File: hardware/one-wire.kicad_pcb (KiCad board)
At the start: 2 copper layers, 30 x 30 mm, 28 parts, among them P1 CON-SENSOR2, P2 DEBUG, P3 BOOT, P4 CONN_02X03, P5 CONN_01X03, U1 XMC1100-16, U2 NC7WZ07, U3 DRILL, U4 DRILL, U5 DRILL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

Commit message: add z diode hint
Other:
- board text added: "5.6V SOD80?"
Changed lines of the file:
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@@
-(kicad_pcb (version 4) (host pcbnew 4.0.2+dfsg1-stable)
+(kicad_pcb (version 4) (host pcbnew 4.0.7-e2-6376~61~ubuntu18.04.1)
   (general
     (links 56)
     (no_connects 0)
-    (area 132.109499 109.509499 162.490501 139.890501)
+    (area 11.95714 108.844999 163.155001 195.615)
     (thickness 1.6)
-    (drawings 20)
+    (drawings 21)
     (tracks 205)
     (zones 0)
@@
     )
   )
+  (gr_text "5.6V SOD80?" (at 149.9 128.1) (layer Dwgs.User)
+    (effects (font (size 2.032 1.524) (thickness 0.3048)))
+  )
   (gr_text VCC (at 139.9 115.3 90) (layer F.SilkS)

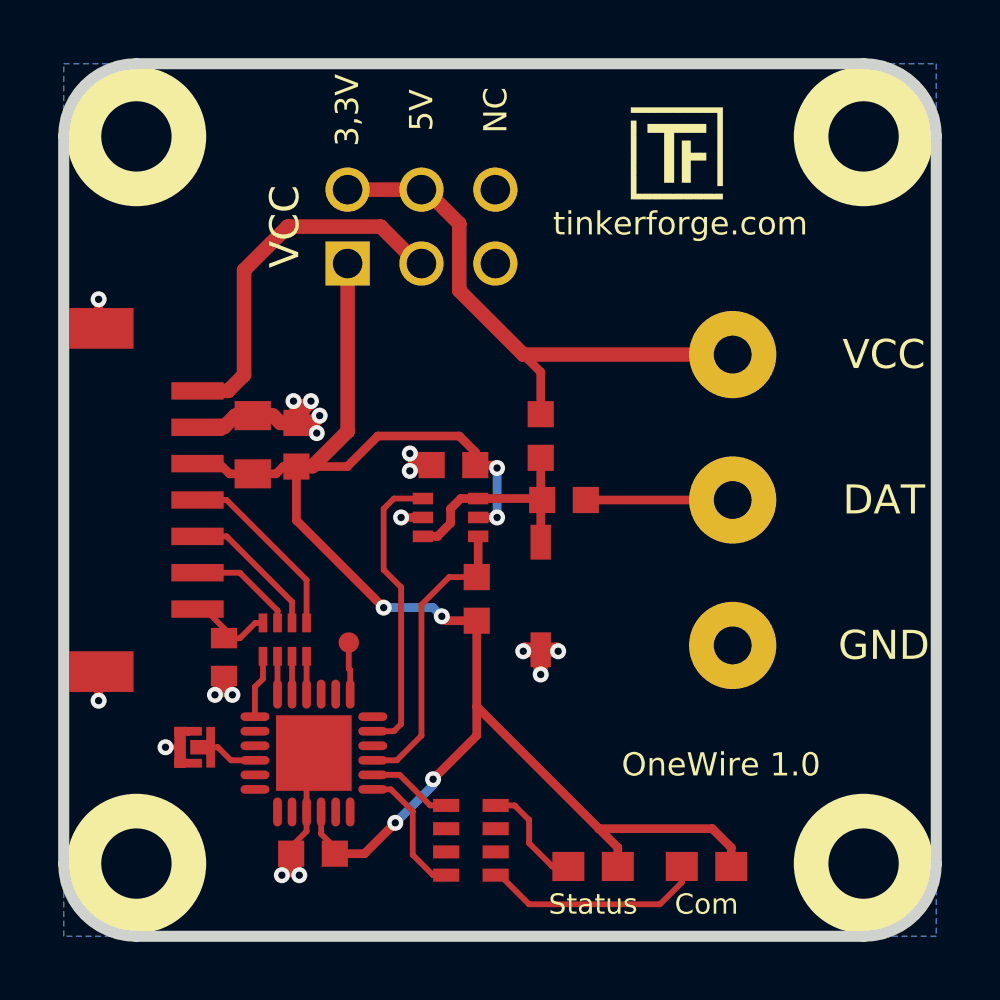
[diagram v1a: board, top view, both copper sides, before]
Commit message: set origin, specify zener
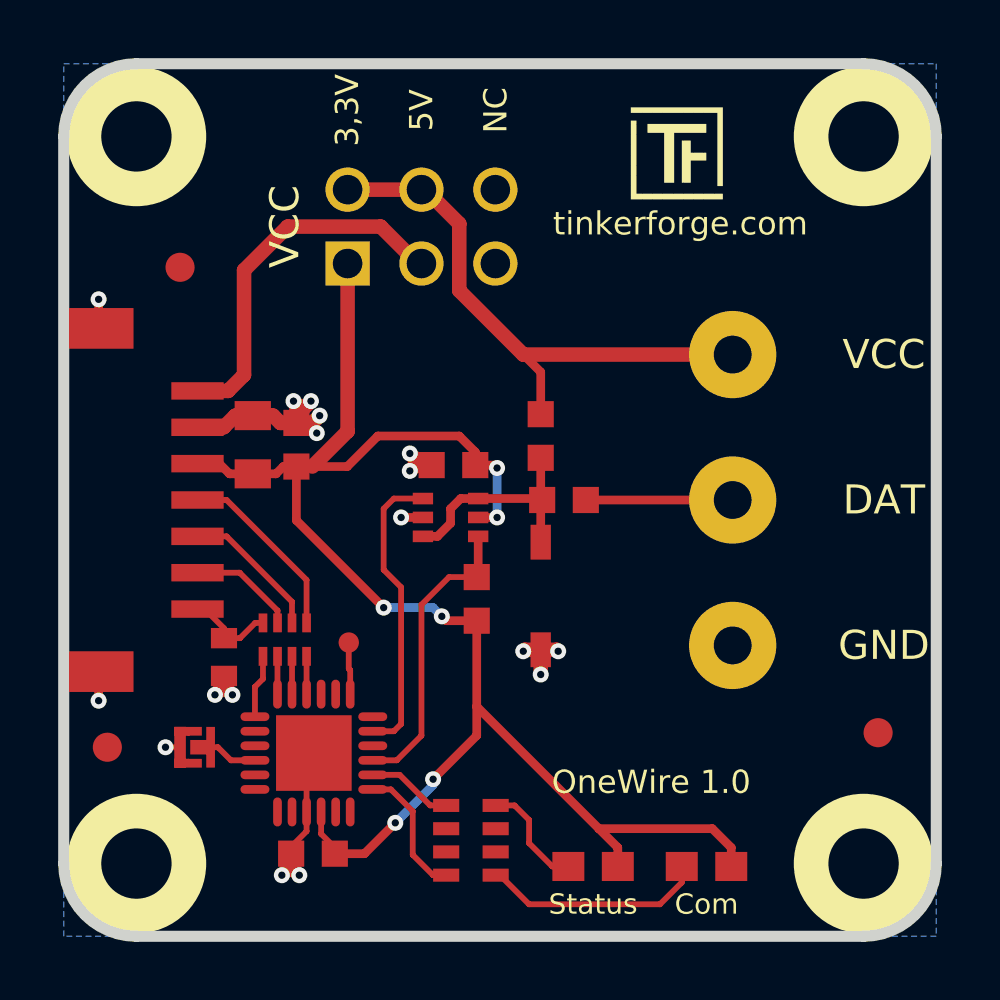
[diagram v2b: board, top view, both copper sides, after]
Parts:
- added Fiducial_Mark: VAL**, kicad-libraries:Fiducial_Mark, F.Cu at (136.3, 116.7)
- added Fiducial_Mark: VAL**, kicad-libraries:Fiducial_Mark, F.Cu at (160.3, 132.7)
- added Fiducial_Mark: VAL**, kicad-libraries:Fiducial_Mark, F.Cu at (133.8, 133.2)
- D2: value ZENER -> 5V
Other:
- board text removed: "5.6V SOD80?"
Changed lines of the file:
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@@
     (area 11.95714 108.844999 163.155001 195.615)
     (thickness 1.6)
-    (drawings 21)
+    (drawings 20)
     (tracks 205)
     (zones 0)
-    (modules 28)
+    (modules 31)
     (nets 23)
   )
@@
   (layers
     (0 F.Cu signal)
-    (31 B.Cu signal)
+    (31 B.Cu signal hide)
     (32 B.Adhes user)
     (33 F.Adhes user)
@@
     (pad_drill 0.6)
     (pad_to_mask_clearance 0)
-    (aux_axis_origin 0 0)
-    (visible_elements FFFFFF7F)
+    (aux_axis_origin 132.3 109.7)
+    (grid_origin 132.3 109.7)
+    (visible_elements FFFF7F7F)
     (pcbplotparams
       (layerselection 0x00010_00000000)
@@
       (effects (font (size 0.2 0.2) (thickness 0.05)))
     )
-    (fp_text value ZENER (at -0.5 -0.54 90) (layer F.Fab)
+    (fp_text value 5V (at -0.5 -0.54 90) (layer F.Fab)
       (effects (font (size 0.2 0.2) (thickness 0.05)))
     )
@@
     )
   )
-  (gr_text "5.6V SOD80?" (at 149.9 128.1) (layer Dwgs.User)
-    (effects (font (size 2.032 1.524) (thickness 0.3048)))
+  (module kicad-libraries:Fiducial_Mark (layer F.Cu)
+    (at 136.3 116.7)
+    (attr smd)
+    (fp_text reference Fiducial_Mark (at 0 0) (layer F.SilkS) hide
+      (effects (font (size 0.127 0.127) (thickness 0.03302)))
+    )
+    (fp_text value VAL** (at 0 -0.29972) (layer F.SilkS) hide
+      (effects (font (size 0.127 0.127) (thickness 0.03302)))
+    )
+    (fp_circle (center 0 0) (end 1.15062 0) (layer Dwgs.User) (width 0.01016))
+    (pad 1 smd circle (at 0 0) (size 1.00076 1.00076) (layers F.Cu F.Paste F.Mask)
+      (clearance 0.65024))
+  )
+  (module kicad-libraries:Fiducial_Mark (layer F.Cu)
+    (at 160.3 132.7)
+    (attr smd)
+    (fp_text reference Fiducial_Mark (at 0 0) (layer F.SilkS) hide
+      (effects (font (size 0.127 0.127) (thickness 0.03302)))
+    )
+    (fp_text value VAL** (at 0 -0.29972) (layer F.SilkS) hide
+      (effects (font (size 0.127 0.127) (thickness 0.03302)))
+    )
+    (fp_circle (center 0 0) (end 1.15062 0) (layer Dwgs.User) (width 0.01016))
+    (pad 1 smd circle (at 0 0) (size 1.00076 1.00076) (layers F.Cu F.Paste F.Mask)
+      (clearance 0.65024))
+  )
+  (module kicad-libraries:Fiducial_Mark (layer F.Cu)
+    (at 133.8 133.2)
+    (attr smd)
+    (fp_text reference Fiducial_Mark (at 0 0) (layer F.SilkS) hide
+      (effects (font (size 0.127 0.127) (thickness 0.03302)))
+    )
+    (fp_text value VAL** (at 0 -0.29972) (layer F.SilkS) hide
+      (effects (font (size 0.127 0.127) (thickness 0.03302)))
+    )
+    (fp_circle (center 0 0) (end 1.15062 0) (layer Dwgs.User) (width 0.01016))
+    (pad 1 smd circle (at 0 0) (size 1.00076 1.00076) (layers F.Cu F.Paste F.Mask)
+      (clearance 0.65024))
   )
   (gr_text VCC (at 139.9 115.3 90) (layer F.SilkS)
@@
     (effects (font (size 0.8 0.8) (thickness 0.15)))
   )
-  (gr_text "OneWire 1.0" (at 154.9 133.8) (layer F.SilkS)
+  (gr_text "OneWire 1.0" (at 152.5 134.4) (layer F.SilkS)
     (effects (font (size 0.8 0.8) (thickness 0.15)))
   )

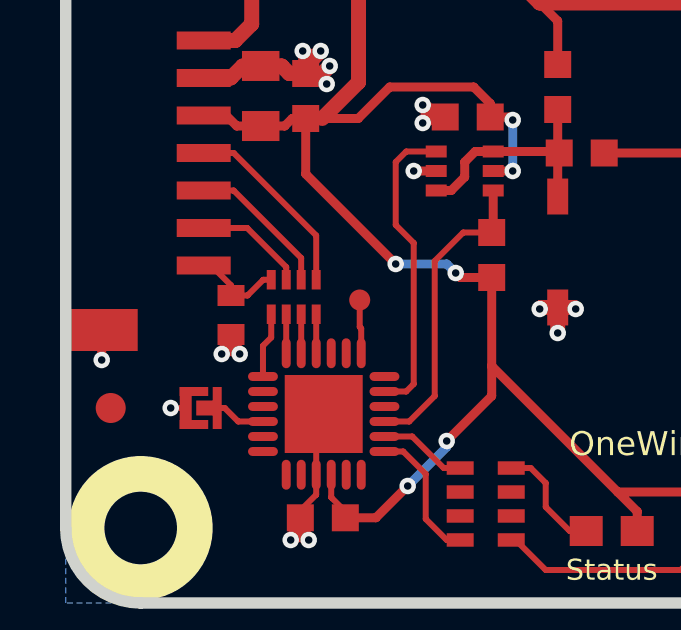
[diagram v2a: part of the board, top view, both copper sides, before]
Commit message: Change capacitor footprint(s) to C0402F
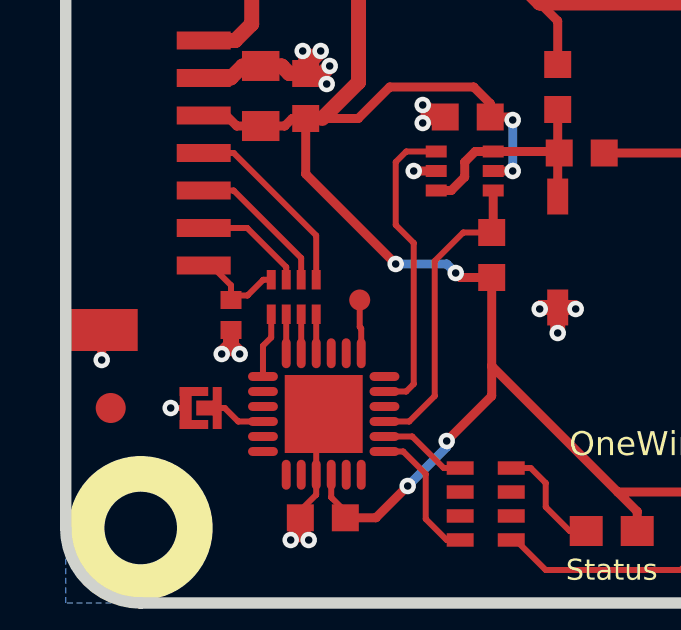
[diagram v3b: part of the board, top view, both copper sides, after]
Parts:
- C2: footprint kicad-libraries:C0402E -> kicad-libraries:C0402F
- R1: footprint R0603F -> kicad-libraries:R0603F
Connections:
- P4 pad 5: (no net) -> Net-(P4-Pad5)
- P4 pad 6: (no net) -> Net-(P4-Pad6)
- RP2 pad 2: (no net) -> Net-(RP2-Pad2)
- RP2 pad 3: (no net) -> Net-(RP2-Pad3)
- RP2 pad 6: (no net) -> Net-(RP2-Pad6)
- RP2 pad 7: (no net) -> Net-(RP2-Pad7)
- U1 pad 11: (no net) -> Net-(U1-Pad11)
- U1 pad 12: (no net) -> Net-(U1-Pad12)
- U1 pad 16: (no net) -> Net-(U1-Pad16)
- U1 pad 18: (no net) -> Net-(U1-Pad18)
- U1 pad 2: (no net) -> Net-(U1-Pad2)
- U1 pad 20: (no net) -> Net-(U1-Pad20)
- U1 pad 21: (no net) -> Net-(U1-Pad21)
- U1 pad 3: (no net) -> Net-(U1-Pad3)
- U1 pad 5: (no net) -> Net-(U1-Pad5)
- U1 pad 6: (no net) -> Net-(U1-Pad6)
- U1 pad 7: (no net) -> Net-(U1-Pad7)
- U1 pad 8: (no net) -> Net-(U1-Pad8)

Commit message: respecify processor XMC1100 -> 1300
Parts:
- U1: value XMC1100-16 -> XMC13XX24
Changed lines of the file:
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@@
-(kicad_pcb (version 4) (host pcbnew 4.0.2+dfsg1-stable)
+(kicad_pcb (version 4) (host pcbnew 4.0.7-e2-6376~61~ubuntu18.04.1)
   (general
     (links 56)
     (no_connects 0)
-    (area 132.109499 109.509499 162.490501 139.890501)
+    (area 11.95714 108.844999 163.155001 195.615)
     (thickness 1.6)
     (drawings 20)
@@
       (effects (font (size 0.3 0.3) (thickness 0.075)))
     )
-    (fp_text value XMC1100-16 (at 0 0.8) (layer F.Fab)
+    (fp_text value XMC13XX24 (at 0 0.8) (layer F.Fab)
       (effects (font (size 0.3 0.3) (thickness 0.075)))
     )

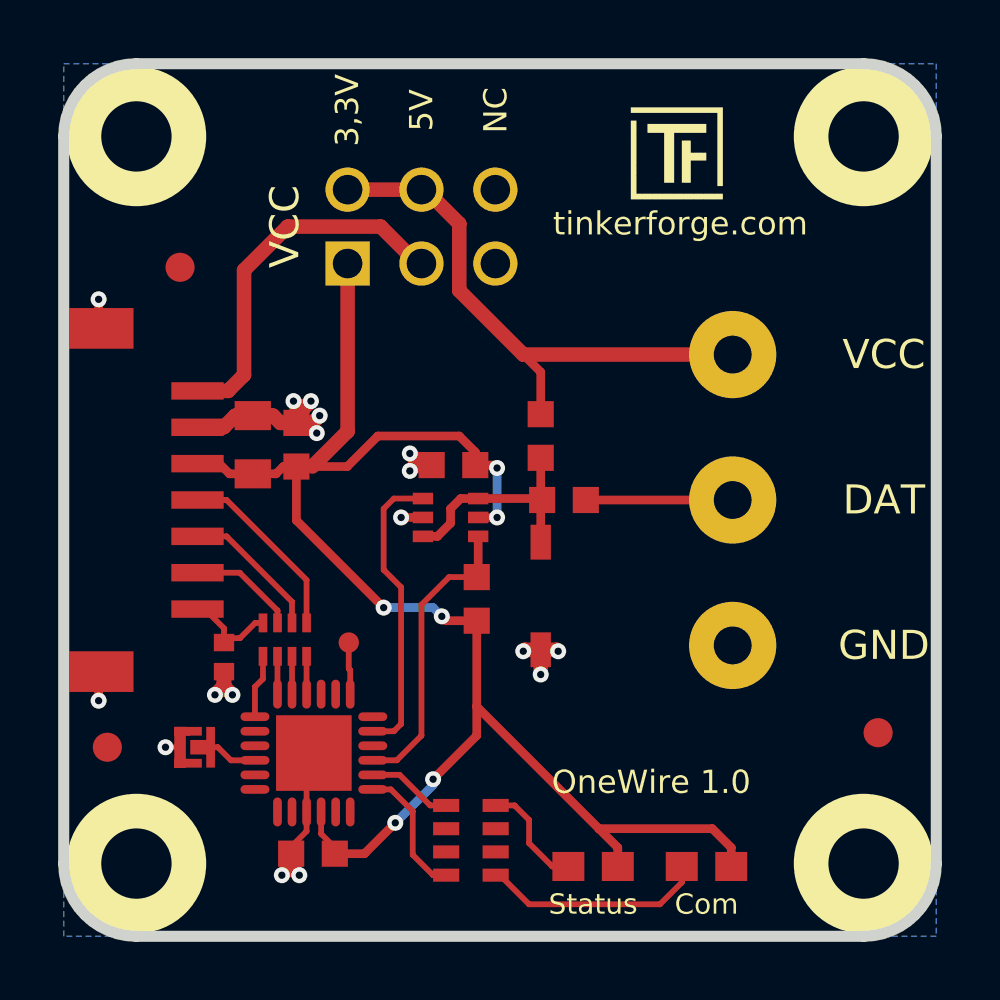
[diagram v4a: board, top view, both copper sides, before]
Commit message: change protection diode to minimelf
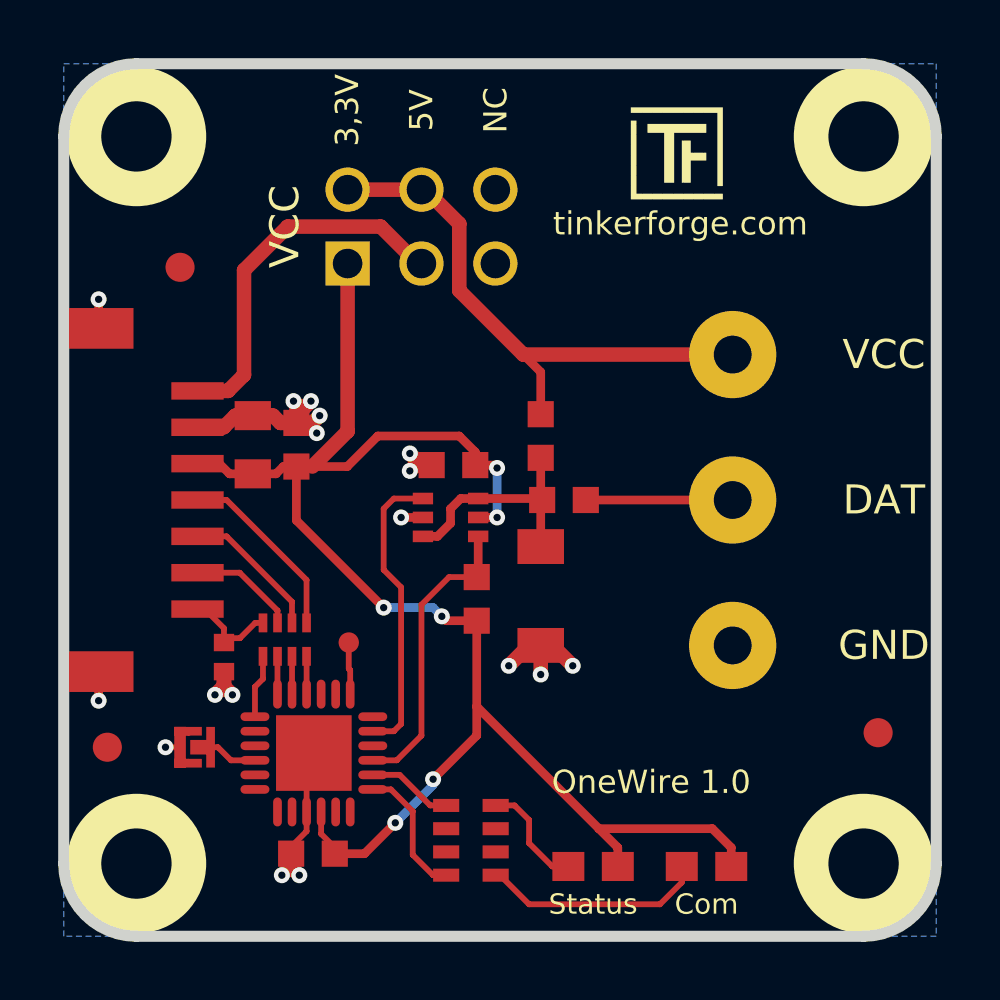
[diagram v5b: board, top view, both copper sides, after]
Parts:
- D2: footprint kicad-libraries:SOD-123 -> kicad-libraries:MiniMelf
- turned D2 to 270 degrees
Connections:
- P4 pad 5: Net-(P4-Pad5) -> (no net)
- P4 pad 6: Net-(P4-Pad6) -> (no net)
- RP2 pad 2: Net-(RP2-Pad2) -> (no net)
- RP2 pad 3: Net-(RP2-Pad3) -> (no net)
- RP2 pad 6: Net-(RP2-Pad6) -> (no net)
- RP2 pad 7: Net-(RP2-Pad7) -> (no net)
- U1 pad 11: Net-(U1-Pad11) -> (no net)
- U1 pad 12: Net-(U1-Pad12) -> (no net)
- U1 pad 16: Net-(U1-Pad16) -> (no net)
- U1 pad 18: Net-(U1-Pad18) -> (no net)
- U1 pad 2: Net-(U1-Pad2) -> (no net)
- U1 pad 20: Net-(U1-Pad20) -> (no net)
- U1 pad 21: Net-(U1-Pad21) -> (no net)
- U1 pad 3: Net-(U1-Pad3) -> (no net)
- U1 pad 5: Net-(U1-Pad5) -> (no net)
- U1 pad 6: Net-(U1-Pad6) -> (no net)
- U1 pad 7: Net-(U1-Pad7) -> (no net)
- U1 pad 8: Net-(U1-Pad8) -> (no net)
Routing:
- net GND: track 27.6 -> 29.0 mm

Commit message: fix one wire routing
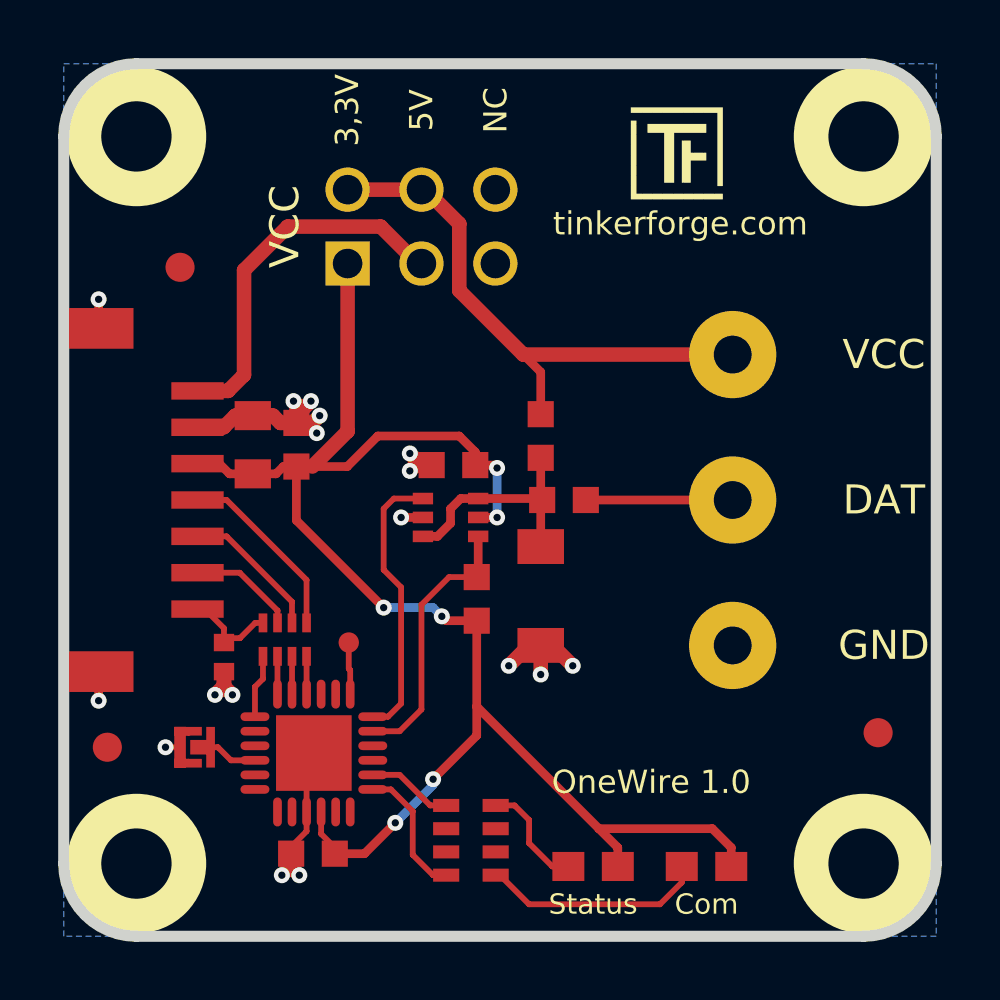
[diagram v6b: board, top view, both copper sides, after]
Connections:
- P1 pad 1: +5V -> (no net)
- P4 pad 2: VCC -> Net-(P4-Pad2)
- P4 pad 3: +5V -> (no net)
- P4 pad 4: VCC -> Net-(P4-Pad2)
- P5 pad 1: VCC -> (no net)
- R2 pad 1: VCC -> (no net)
- U1 pad 15: RX -> (no net)
- U1 pad 17: TX -> RX
- U1 pad 18: (no net) -> TX
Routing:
- net VCC: track 19.2 -> 0.00 mm
- net Net-(P4-Pad2): track 0.00 -> 19.2 mm
- net +5V: track 12.7 -> 0.00 mm
- net (no net): track 0.00 -> 12.7 mm
- net RX: track 10.2 -> 9.30 mm
- net TX: track 10.2 -> 9.60 mm
